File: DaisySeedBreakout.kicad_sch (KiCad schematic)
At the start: 34 parts, among them J2 Conn_01x02, J24 Conn_01x02, J25 Conn_01x02, J26 Conn_02x04, J30 Conn_01x02, J31 Conn_02x04, J32 Conn_01x02, J33 Conn_01x02, J34 Conn_01x02, J35 Conn_01x02, J6 Conn_01x02, U7 LM317MDCYR

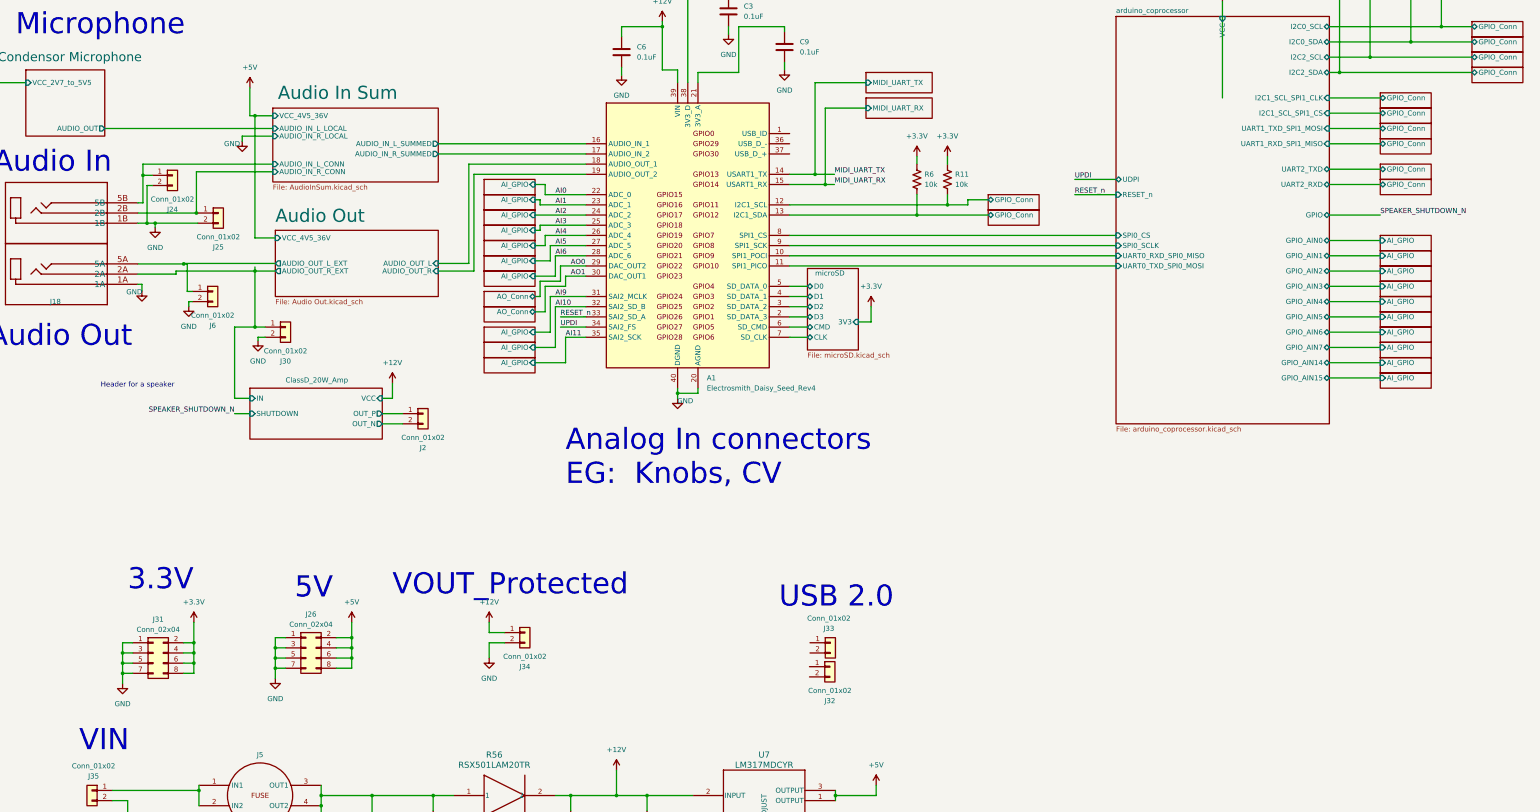
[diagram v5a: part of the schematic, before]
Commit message: add usb host current limit and ESD diodes
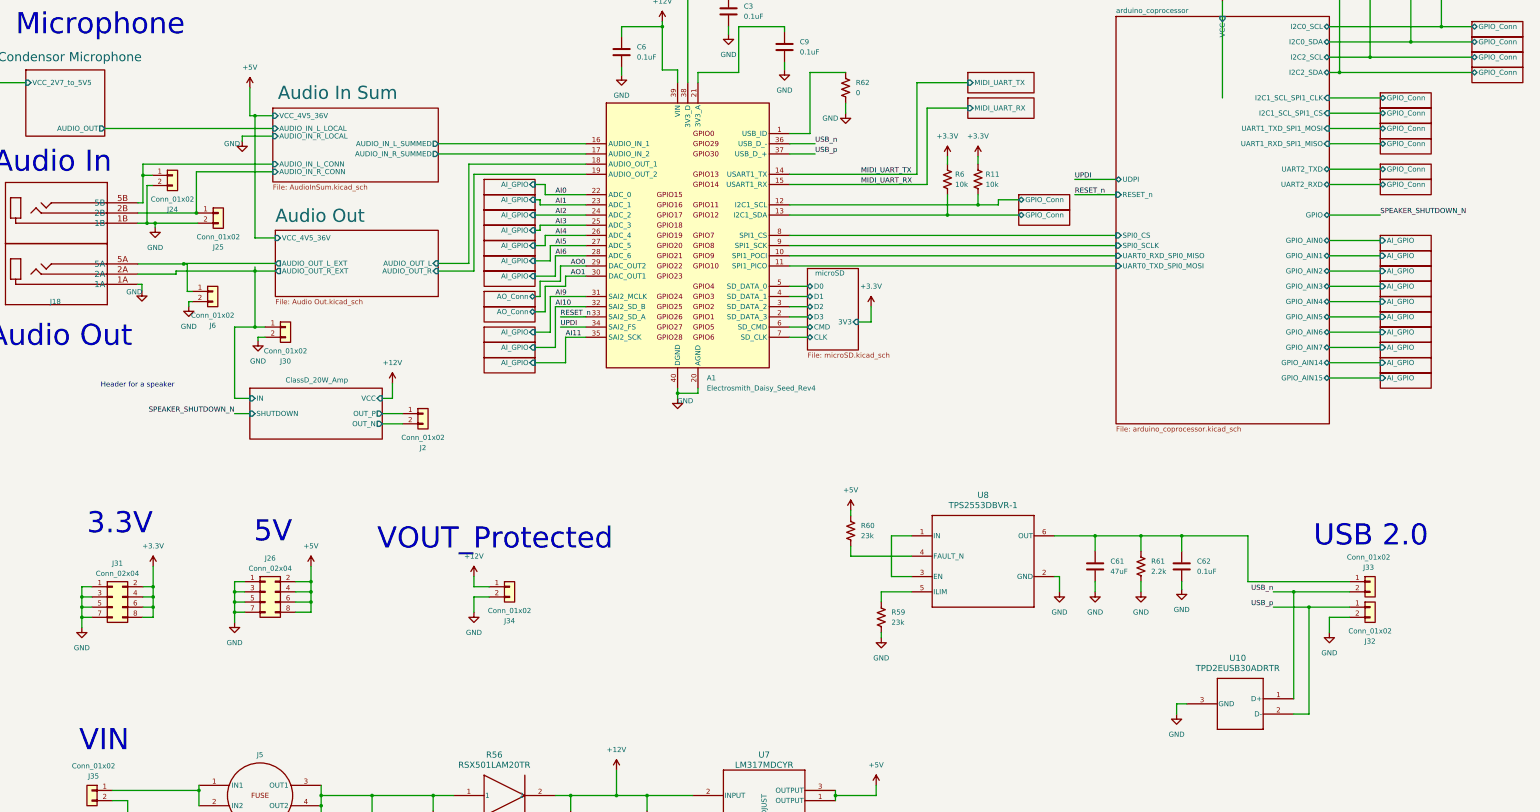
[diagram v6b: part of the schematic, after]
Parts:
- added C61: 47uF, Capacitor_SMD:C_0805_2012Metric, symbol Device:C
- added C62: 0.1uF, Capacitor_SMD:C_0402_1005Metric, symbol Device:C
- added R59, R60: 23k, Resistor_SMD:R_0402_1005Metric, symbol Device:R_US
- added R61: 2.2k, Resistor_SMD:R_0402_1005Metric, symbol Device:R_US
- added R62: 0, Resistor_SMD:R_0402_1005Metric, symbol Device:R_US
- added U10: TPD2EUSB30ADRTR, DRT3, symbol 2023-10-02_10-27-03:TPD2EUSB30ADRTR
- added U8: TPS2553DBVR-1, DBV0006A_N, symbol 2023-10-02_10-29-40:TPS2553DBVR-1
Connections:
- net +5V: now also R60.1
- net GND: now also J32.2 (Pin_2), C61.2, C62.2, R59.2, R61.2, R62.2, U10.3 (GND), U8.2 (GND)
- net at J33.1 (Pin_1): now also C61.1, C62.1, R61.1, U8.6 (OUT)
- net USB_n: now reaches J33.2 (Pin_2)
- net USB_n: now also A1.36 (USB_D_-), U10.1 (D+)
- net at A1.1 (USB_ID): now also R62.1
- net USB_p: now reaches A1.37 (USB_D_+)
- net USB_p: now also J32.1 (Pin_1), U10.2 (D-)
- new net: R59.1, U8.5 (ILIM)
- new net: R60.2, U8.4 (FAULT_N)
- new net: U8.1 (IN), U8.3 (EN)
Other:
- note removed: "Analog In connectors EG: Knobs, CV"
- moved on the sheet: J26, J31, J32, J33, J34, R11, R6

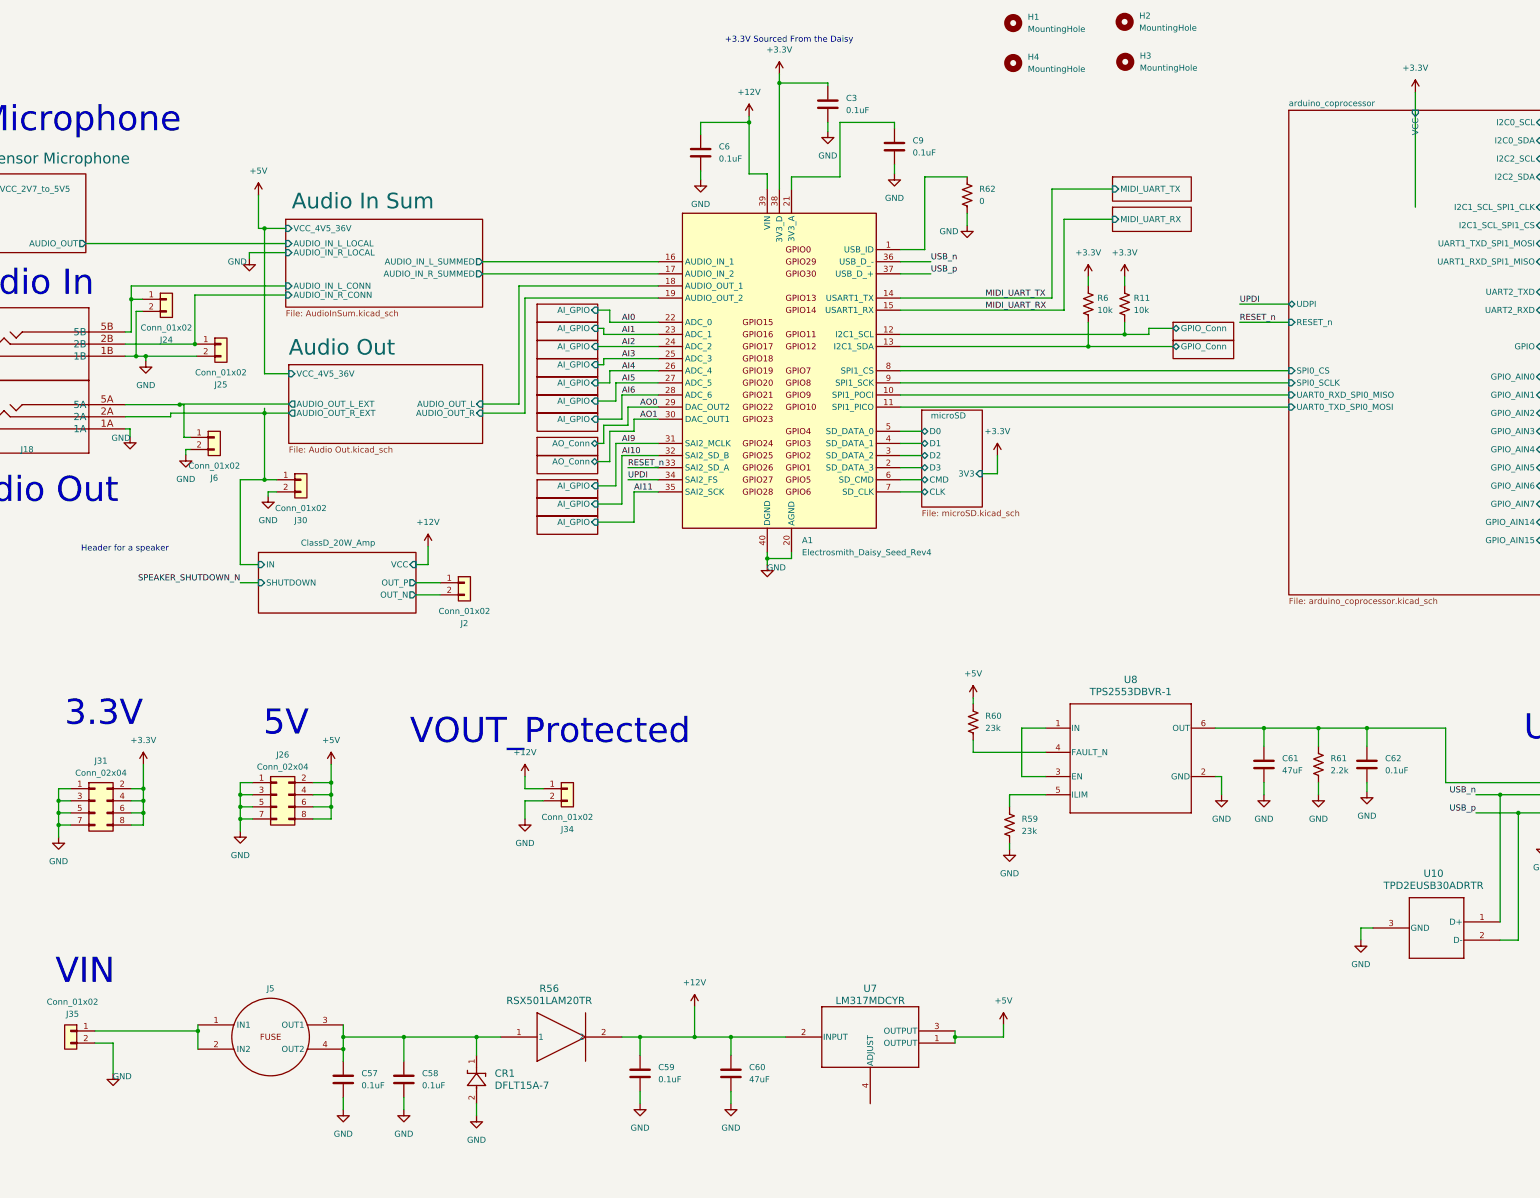
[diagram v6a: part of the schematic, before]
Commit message: Add USB 5V switcher, adjust audio in circuit
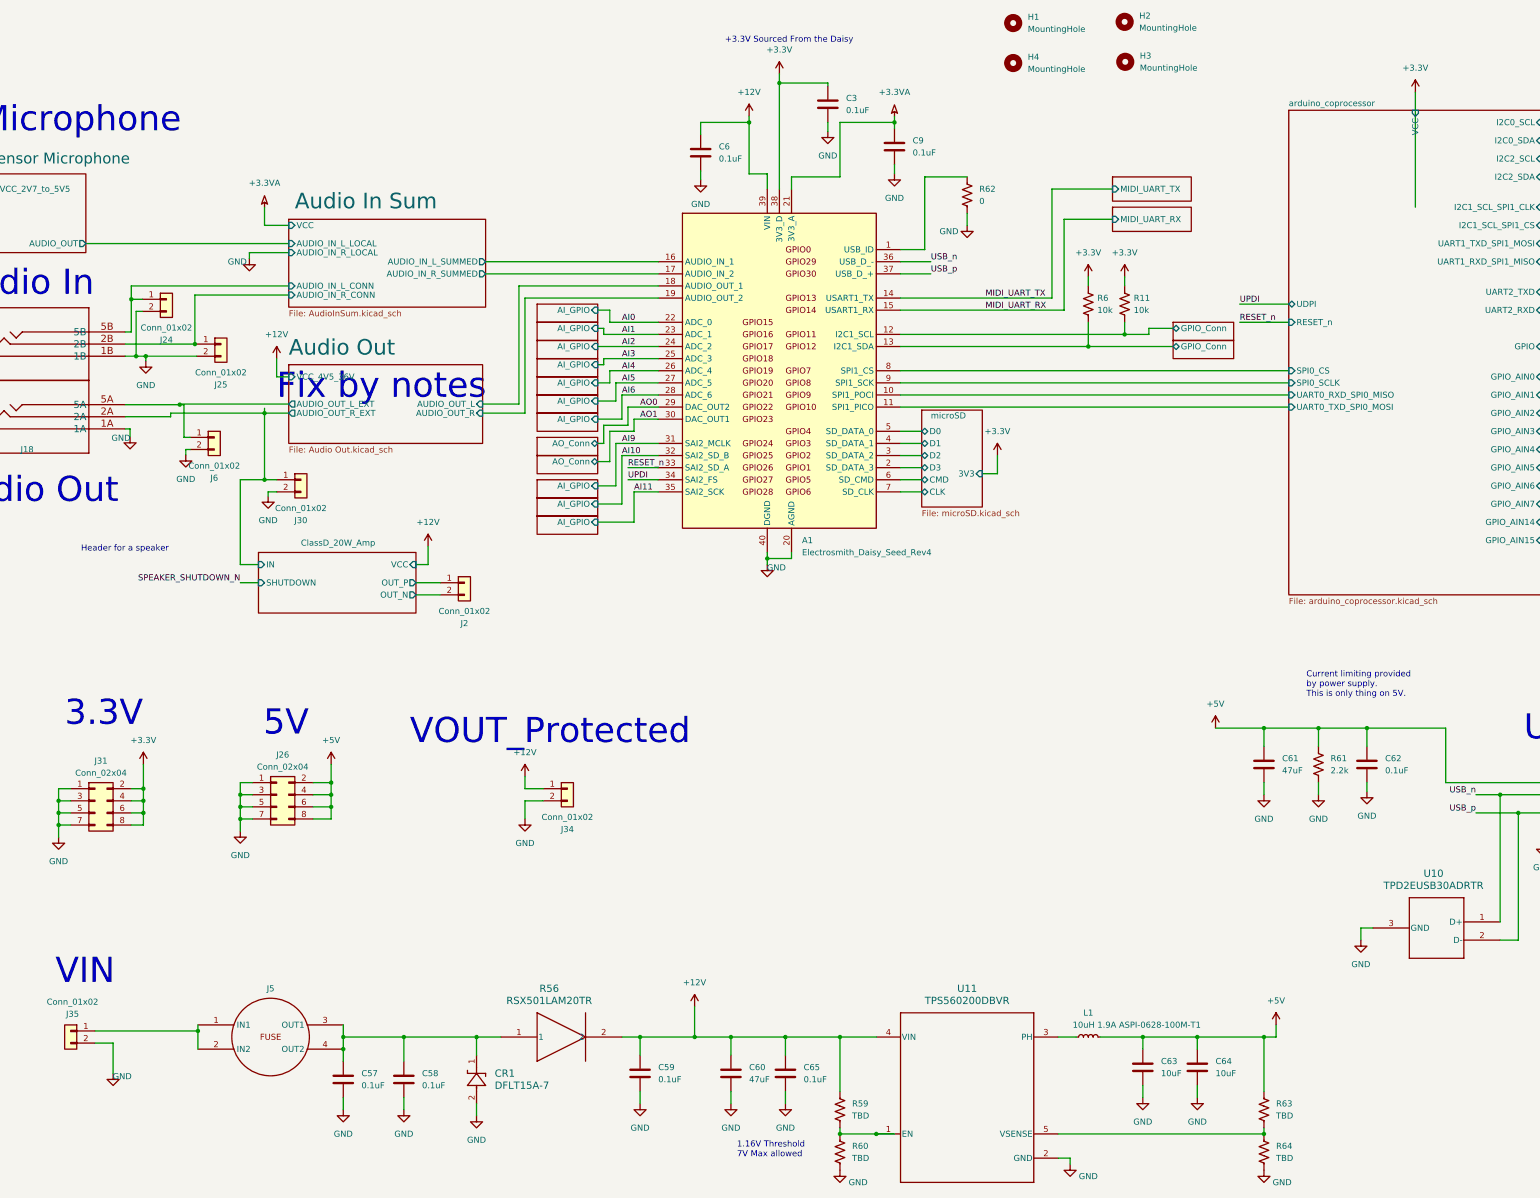
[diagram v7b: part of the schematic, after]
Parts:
- removed U7: LM317MDCYR, DCY4, symbol 2023-10-02_00-54-17:LM317MDCYR
- removed U8: TPS2553DBVR-1, DBV0006A_N, symbol 2023-10-02_10-29-40:TPS2553DBVR-1
- added C63, C64: 10uF, Capacitor_SMD:C_0603_1608Metric, symbol Device:C
- added C65: 0.1uF, Capacitor_SMD:C_0402_1005Metric, symbol Device:C
- added L1: 10uH 1.9A ASPI-0628-100M-T1, 10uHInductor:ASPI-0628_ASPI-0628-4R7M-T1_ABR, symbol Device:L_Small
- added R63, R64: TBD, Resistor_SMD:R_0402_1005Metric, symbol Device:R_US
- added U11: TPS560200DBVR, DBV0005A_N, symbol 2023-10-05_01-44-07:TPS560200DBVR
- R59, R60: value 23k -> TBD
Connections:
- net +12V: now also R59.1, C65.1, U11.4 (VIN)
- net +5V: now also C61.1, C62.1, J33.1 (Pin_1), R61.1, C63.1, C64.1, L1.2, R63.1; no longer R60.1
- net GND: now also R60.2, C63.2, C64.2, C65.2, R64.2, U11.2 (GND); no longer R59.2
- net +3.3VA: now reaches A1.21 (3V3_A), C9.1
- new net: R59.2, R60.1, U11.1 (EN)
- new net: L1.1, U11.3 (PH)
- new net: R63.2, R64.1, U11.5 (VSENSE)
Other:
- sheet Audio In Sum ports: added VCC; removed VCC_4V5_36V
- note added: "1.16V Threshold 7V Max allowed"
- note added: "Current limiting provided by power supply. This is only thing on 5V."
- note added: "Fix by notes"
